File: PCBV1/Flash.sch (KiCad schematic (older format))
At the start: 0 parts

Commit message: Added SD filter and USB-to-UART IC.
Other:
- note added: "some n25 type, 128 Mb"
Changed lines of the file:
@@
 $Descr A4 11693 8268
 encoding utf-8
-Sheet 5 8
+Sheet 4 8
 Title "Smart Mirror"
-Date "2021-01-21"
+Date "2022-04-22"
 Rev "1.0"
 Comp "University of Southern Denmark"
@@
 Comment4 ""
 $EndDescr
+Text Notes 5300 3850 0    50   ~ 0
+some n25 type, 128 Mb
 $EndSCHEMATC

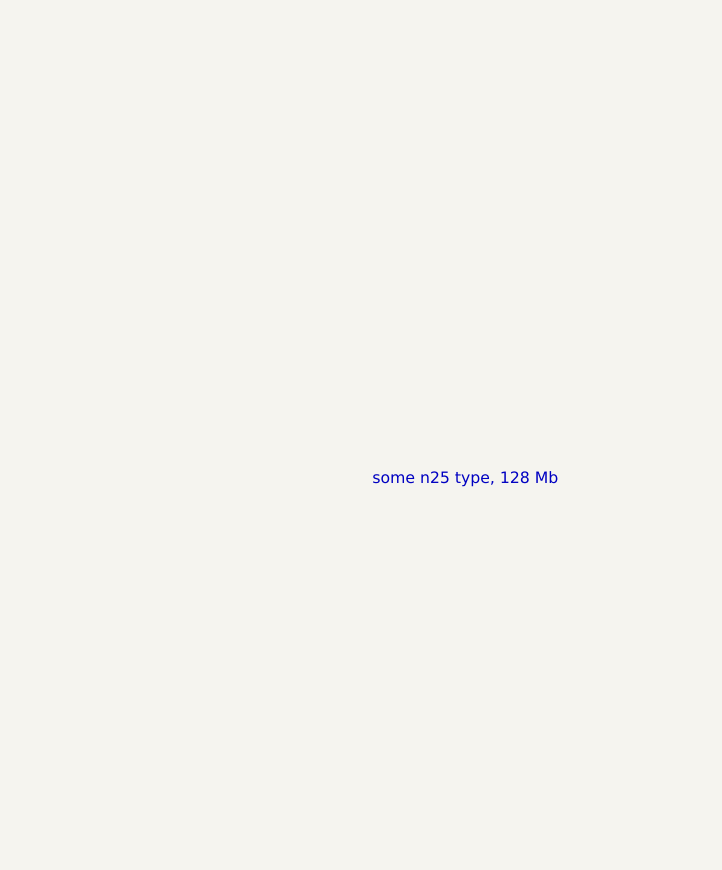
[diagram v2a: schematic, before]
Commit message: Added NAND flash with connections, updated IO config.
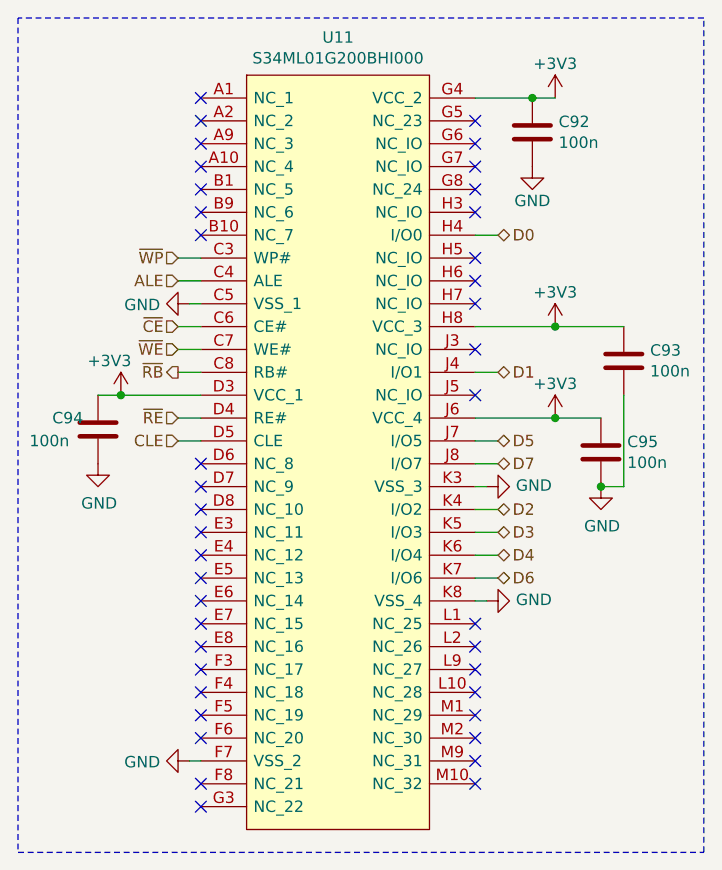
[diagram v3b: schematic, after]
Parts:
- added C92, C93, C94, C95: 100n, Capacitor_SMD:C_0603_1608Metric, symbol Device:C
- added U11: S34ML01G200BHI000, Personal_ICs:S34ML01G200BHI000, symbol Personal_ICs:S34ML01G200BHI000
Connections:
- new net +3V3: C92.1, C93.1, C94.1, C95.1, U11.D3 (VCC_1), U11.G4 (VCC_2), U11.H8 (VCC_3), U11.J6 (VCC_4)
- new net ALE: U11.C4 (ALE)
- new net CLE: U11.D5 (CLE)
- new net D0: U11.H4 (I/O0)
- new net D1: U11.J4 (I/O1)
- new net D2: U11.K4 (I/O2)
- new net D3: U11.K5 (I/O3)
- new net D4: U11.K6 (I/O4)
- new net D5: U11.J7 (I/O5)
- new net D6: U11.K7 (I/O6)
- new net D7: U11.J8 (I/O7)
- new net GND: C92.2, C93.2, C94.2, C95.2, U11.C5 (VSS_1), U11.F7 (VSS_2), U11.K3 (VSS_3), U11.K8 (VSS_4)
- new net ~CE: U11.C6 (CE#)
- new net ~RB: U11.C8 (RB#)
- new net ~RE: U11.D4 (RE#)
- new net ~WE: U11.C7 (WE#)
- new net ~WP: U11.C3 (WP#)
- no-connect marks 0 -> 40
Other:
- note removed: "some n25 type, 128 Mb"

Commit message: Laid final hands on Wi-Fi and all circuits. Started work on PCB.
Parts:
- renumbered C92 to C30, C93 to C31, C94 to C32, C95 to C33, U11 to U8
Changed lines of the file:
@@
 Sheet 4 8
 Title "Smart Mirror"
-Date "2022-04-22"
+Date "2022-05-11"
 Rev "1.0"
 Comp "University of Southern Denmark"
@@
 $EndDescr
 $Comp
-L Personal_ICs:S34ML01G200BHI000 U11
+L Personal_ICs:S34ML01G200BHI000 U8
 U 1 1 62CA6EF5
 P 4550 2150
-F 0 "U11" H 5150 2415 50  0000 C CNN
+F 0 "U8" H 5150 2415 50  0000 C CNN
 F 1 "S34ML01G200BHI000" H 5150 2324 50  0000 C CNN
 F 2 "Personal_ICs:S34ML01G200BHI000" H 5600 2250 50  0001 L CNN
@@
 	5750 3950 5850 3950
 $Comp
-L power:GND #PWR0279
+L power:GND #PWR058
 U 1 1 62CB83E0
 P 4500 5050
-F 0 "#PWR0279" H 4500 4800 50  0001 C CNN
+F 0 "#PWR058" H 4500 4800 50  0001 C CNN
 F 1 "GND" V 4505 4922 50  0000 R CNN
 F 2 "" H 4500 5050 50  0001 C CNN
@@
 	4500 5050 4550 5050
 $Comp
-L power:GND #PWR0280
+L power:GND #PWR057
 U 1 1 62CB9252
 P 5800 4350
-F 0 "#PWR0280" H 5800 4100 50  0001 C CNN
+F 0 "#PWR057" H 5800 4100 50  0001 C CNN
 F 1 "GND" V 5805 4222 50  0000 R CNN
 F 2 "" H 5800 4350 50  0001 C CNN
@@
 	5800 4350 5750 4350
 $Comp
-L power:GND #PWR0281
+L power:GND #PWR055
 U 1 1 62CB96EA
 P 5800 3850
-F 0 "#PWR0281" H 5800 3600 50  0001 C CNN
+F 0 "#PWR055" H 5800 3600 50  0001 C CNN
 F 1 "GND" V 5805 3722 50  0000 R CNN
 F 2 "" H 5800 3850 50  0001 C CNN
@@
 	5800 3850 5750 3850
 $Comp
-L power:GND #PWR0282
+L power:GND #PWR050
 U 1 1 62CB9E1A
 P 4500 3050
-F 0 "#PWR0282" H 4500 2800 50  0001 C CNN
+F 0 "#PWR050" H 4500 2800 50  0001 C CNN
 F 1 "GND" V 4505 2922 50  0000 R CNN
 F 2 "" H 4500 3050 50  0001 C CNN
@@
 	4500 3050 4550 3050
 $Comp
-L power:+3V3 #PWR0283
+L power:+3V3 #PWR051
 U 1 1 62CBAD8D
 P 6100 3150
-F 0 "#PWR0283" H 6100 3000 50  0001 C CNN
+F 0 "#PWR051" H 6100 3000 50  0001 C CNN
 F 1 "+3V3" H 6100 3300 50  0000 C CNN
 F 2 "" H 6100 3150 50  0001 C CNN
@@
 	5750 3150 6100 3150
 $Comp
-L power:+3V3 #PWR0284
+L power:+3V3 #PWR053
 U 1 1 62CBC93E
 P 6100 3550
-F 0 "#PWR0284" H 6100 3400 50  0001 C CNN
+F 0 "#PWR053" H 6100 3400 50  0001 C CNN
 F 1 "+3V3" H 6100 3700 50  0000 C CNN
 F 2 "" H 6100 3550 50  0001 C CNN
@@
 	5750 3550 6100 3550
 $Comp
-L power:+3V3 #PWR0285
+L power:+3V3 #PWR052
 U 1 1 62CBD4E6
 P 4200 3450
-F 0 "#PWR0285" H 4200 3300 50  0001 C CNN
+F 0 "#PWR052" H 4200 3300 50  0001 C CNN
 F 1 "+3V3" H 4150 3600 50  0000 C CNN
 F 2 "" H 4200 3450 50  0001 C CNN
@@
 	4550 3450 4200 3450
 $Comp
-L power:+3V3 #PWR0286
+L power:+3V3 #PWR048
 U 1 1 62CBE2F7
 P 6100 2150
-F 0 "#PWR0286" H 6100 2000 50  0001 C CNN
+F 0 "#PWR048" H 6100 2000 50  0001 C CNN
 F 1 "+3V3" H 6100 2300 50  0000 C CNN
 F 2 "" H 6100 2150 50  0001 C CNN
@@
 	5750 2150 6000 2150
 $Comp
-L Device:C C92
+L Device:C C30
 U 1 1 62CBF3ED
 P 6000 2300
-F 0 "C92" H 6115 2346 50  0000 L CNN
+F 0 "C30" H 6115 2346 50  0000 L CNN
 F 1 "100n" H 6115 2255 50  0000 L CNN
 F 2 "Capacitor_SMD:C_0603_1608Metric" H 6038 2150 50  0001 C CNN
@@
 	6000 2150 6100 2150
 $Comp
-L power:GND #PWR0287
+L power:GND #PWR049
 U 1 1 62CBFE60
 P 6000 2450
-F 0 "#PWR0287" H 6000 2200 50  0001 C CNN
+F 0 "#PWR049" H 6000 2200 50  0001 C CNN
 F 1 "GND" H 6000 2300 50  0000 C CNN
 F 2 "" H 6000 2450 50  0001 C CNN
@@
 $EndComp
 $Comp
-L Device:C C93
+L Device:C C31
 U 1 1 62CC1503
 P 6400 3300
-F 0 "C93" H 6515 3346 50  0000 L CNN
+F 0 "C31" H 6515 3346 50  0000 L CNN
 F 1 "100n" H 6515 3255 50  0000 L CNN
 F 2 "Capacitor_SMD:C_0603_1608Metric" H 6438 3150 50  0001 C CNN
@@
 $EndComp
 $Comp
-L Device:C C95
+L Device:C C33
 U 1 1 62CC3177
 P 6300 3700
-F 0 "C95" H 6415 3746 50  0000 L CNN
+F 0 "C33" H 6415 3746 50  0000 L CNN
 F 1 "100n" H 6415 3655 50  0000 L CNN
 F 2 "Capacitor_SMD:C_0603_1608Metric" H 6338 3550 50  0001 C CNN
@@
 Connection ~ 6100 3550
 $Comp
-L power:GND #PWR0288
+L power:GND #PWR056
 U 1 1 62CC46CC
 P 6300 3850
-F 0 "#PWR0288" H 6300 3600 50  0001 C CNN
+F 0 "#PWR056" H 6300 3600 50  0001 C CNN
 F 1 "GND" H 6305 3677 50  0000 C CNN
 F 2 "" H 6300 3850 50  0001 C CNN
@@
 Connection ~ 6300 3850
 $Comp
-L Device:C C94
+L Device:C C32
 U 1 1 62CC7801
 P 4100 3600
-F 0 "C94" H 3900 3650 50  0000 L CNN
+F 0 "C32" H 3900 3650 50  0000 L CNN
 F 1 "100n" H 3800 3550 50  0000 L CNN
 F 2 "Capacitor_SMD:C_0603_1608Metric" H 4138 3450 50  0001 C CNN
@@
 Connection ~ 4200 3450
 $Comp
-L power:GND #PWR0289
+L power:GND #PWR054
 U 1 1 62CC9054
 P 4100 3750
-F 0 "#PWR0289" H 4100 3500 50  0001 C CNN
+F 0 "#PWR054" H 4100 3500 50  0001 C CNN
 F 1 "GND" H 4105 3577 50  0000 C CNN
 F 2 "" H 4100 3750 50  0001 C CNN
